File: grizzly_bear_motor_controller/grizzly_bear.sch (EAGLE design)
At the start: 54 parts, among them Q1 PH7030L, Q2 PH7030L, Q3 PH7030L, Q4 PH7030L, Q5 FDD4141TO252, U1 A4940, U2 ATMEGA32U4-AU, U3 ACS714, U4 UA78L00, Y1 16MHz

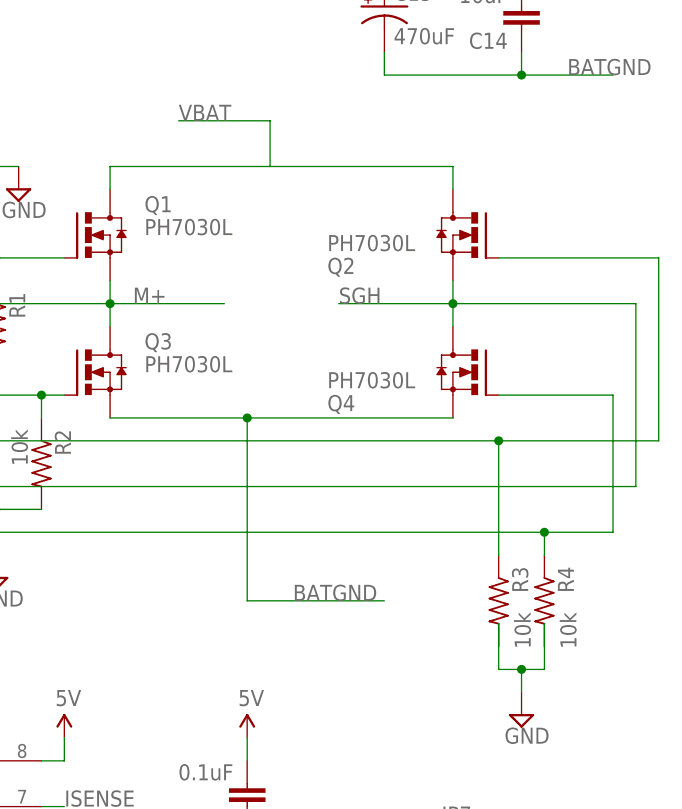
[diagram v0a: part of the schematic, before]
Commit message: Fix mistake with AHI shorted to ENC2
Change-Id: I23787c04aa77e54cc0262fec6cb01ab894f515dc
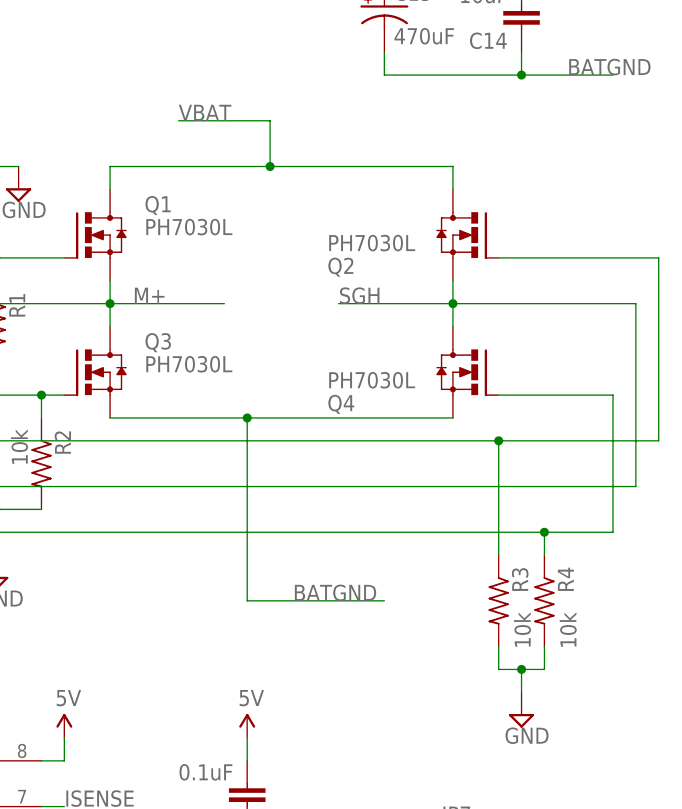
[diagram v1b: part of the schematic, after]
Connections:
- new net AHI: R13.1, U1.AHI, U2.(PCINT6/OC1B/OC4B/ADC13)PB6
- net ENC2: no longer R13.1, U1.AHI, U2.(PCINT6/OC1B/OC4B/ADC13)PB6
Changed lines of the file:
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@@
 <pinref part="Q2" gate="G$1" pin="D"/>
 <wire x1="132.08" y1="93.98" x2="132.08" y2="96.52" width="0.1524" layer="91"/>
+<junction x="111.76" y="96.52"/>
 </segment>
 <segment>
@@
 <wire x1="139.7" y1="40.64" x2="137.16" y2="40.64" width="0.1524" layer="91"/>
 <pinref part="R3" gate="G$1" pin="2"/>
-<wire x1="137.16" y1="45.72" x2="137.16" y2="43.18" width="0.1524" layer="91"/>
 <wire x1="137.16" y1="40.64" x2="137.16" y2="43.18" width="0.1524" layer="91"/>
 <pinref part="R4" gate="G$1" pin="2"/>
-<wire x1="142.24" y1="45.72" x2="142.24" y2="43.18" width="0.1524" layer="91"/>
 <wire x1="142.24" y1="43.18" x2="142.24" y2="40.64" width="0.1524" layer="91"/>
 <wire x1="142.24" y1="40.64" x2="139.7" y2="40.64" width="0.1524" layer="91"/>
@@
 </segment>
 <segment>
-<wire x1="5.08" y1="71.12" x2="15.24" y2="71.12" width="0.1524" layer="91"/>
-<wire x1="15.24" y1="71.12" x2="15.24" y2="81.28" width="0.1524" layer="91"/>
-<wire x1="15.24" y1="81.28" x2="25.4" y2="81.28" width="0.1524" layer="91"/>
-<pinref part="U1" gate="G$1" pin="AHI"/>
-<pinref part="R13" gate="G$1" pin="1"/>
-<wire x1="5.08" y1="58.42" x2="5.08" y2="71.12" width="0.1524" layer="91"/>
-<wire x1="5.08" y1="71.12" x2="-2.54" y2="71.12" width="0.1524" layer="91"/>
-<wire x1="-2.54" y1="71.12" x2="-5.08" y2="68.58" width="0.1524" layer="91"/>
-<wire x1="-5.08" y1="68.58" x2="-10.16" y2="68.58" width="0.1524" layer="91"/>
-<junction x="5.08" y="71.12"/>
-<pinref part="U2" gate="G$1" pin="(PCINT6/OC1B/OC4B/ADC13)PB6"/>
-</segment>
-<segment>
 <wire x1="-10.16" y1="73.66" x2="-7.62" y2="73.66" width="0.1524" layer="91"/>
 <label x="-7.62" y="73.66" size="1.778" layer="95"/>
@@
 </segment>
 </net>
+<net name="AHI" class="0">
+<segment>
+<wire x1="5.08" y1="71.12" x2="15.24" y2="71.12" width="0.1524" layer="91"/>
+<wire x1="15.24" y1="71.12" x2="15.24" y2="81.28" width="0.1524" layer="91"/>
+<wire x1="15.24" y1="81.28" x2="25.4" y2="81.28" width="0.1524" layer="91"/>
+<pinref part="U1" gate="G$1" pin="AHI"/>
+<pinref part="R13" gate="G$1" pin="1"/>
+<wire x1="5.08" y1="58.42" x2="5.08" y2="71.12" width="0.1524" layer="91"/>
+<wire x1="5.08" y1="71.12" x2="-2.54" y2="71.12" width="0.1524" layer="91"/>
+<wire x1="-2.54" y1="71.12" x2="-5.08" y2="68.58" width="0.1524" layer="91"/>
+<wire x1="-5.08" y1="68.58" x2="-10.16" y2="68.58" width="0.1524" layer="91"/>
+<junction x="5.08" y="71.12"/>
+<pinref part="U2" gate="G$1" pin="(PCINT6/OC1B/OC4B/ADC13)PB6"/>
+</segment>
+</net>

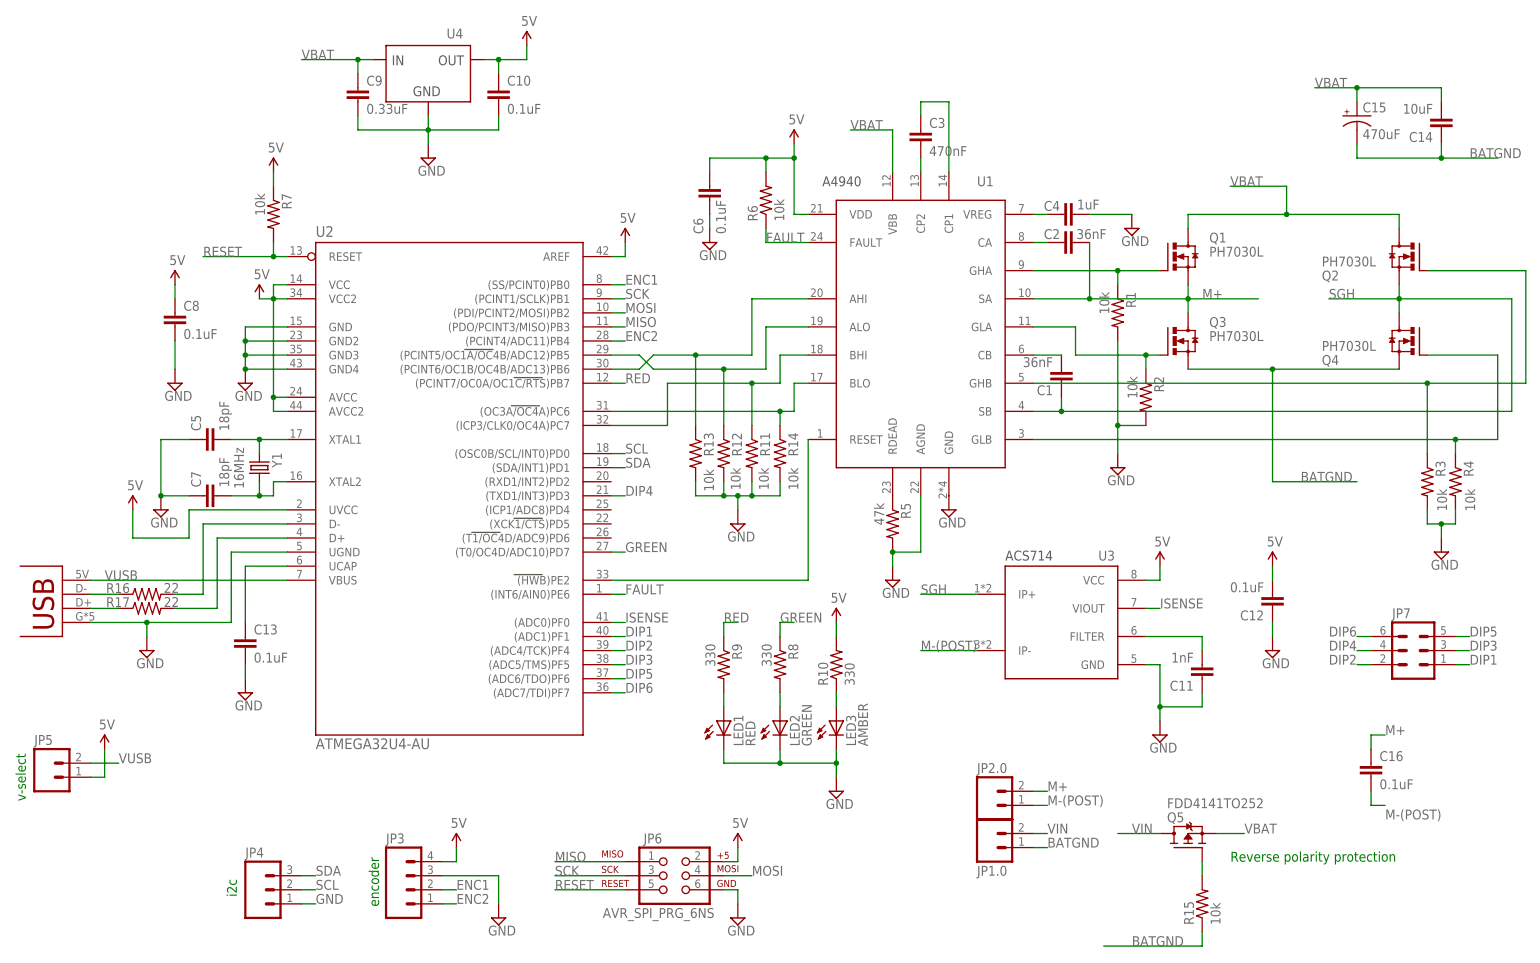
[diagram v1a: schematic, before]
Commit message: Fix 18pF caps and renumber all passives
Change-Id: Id4e7dc3682557a51dcb971b0b6fbe1525da739df
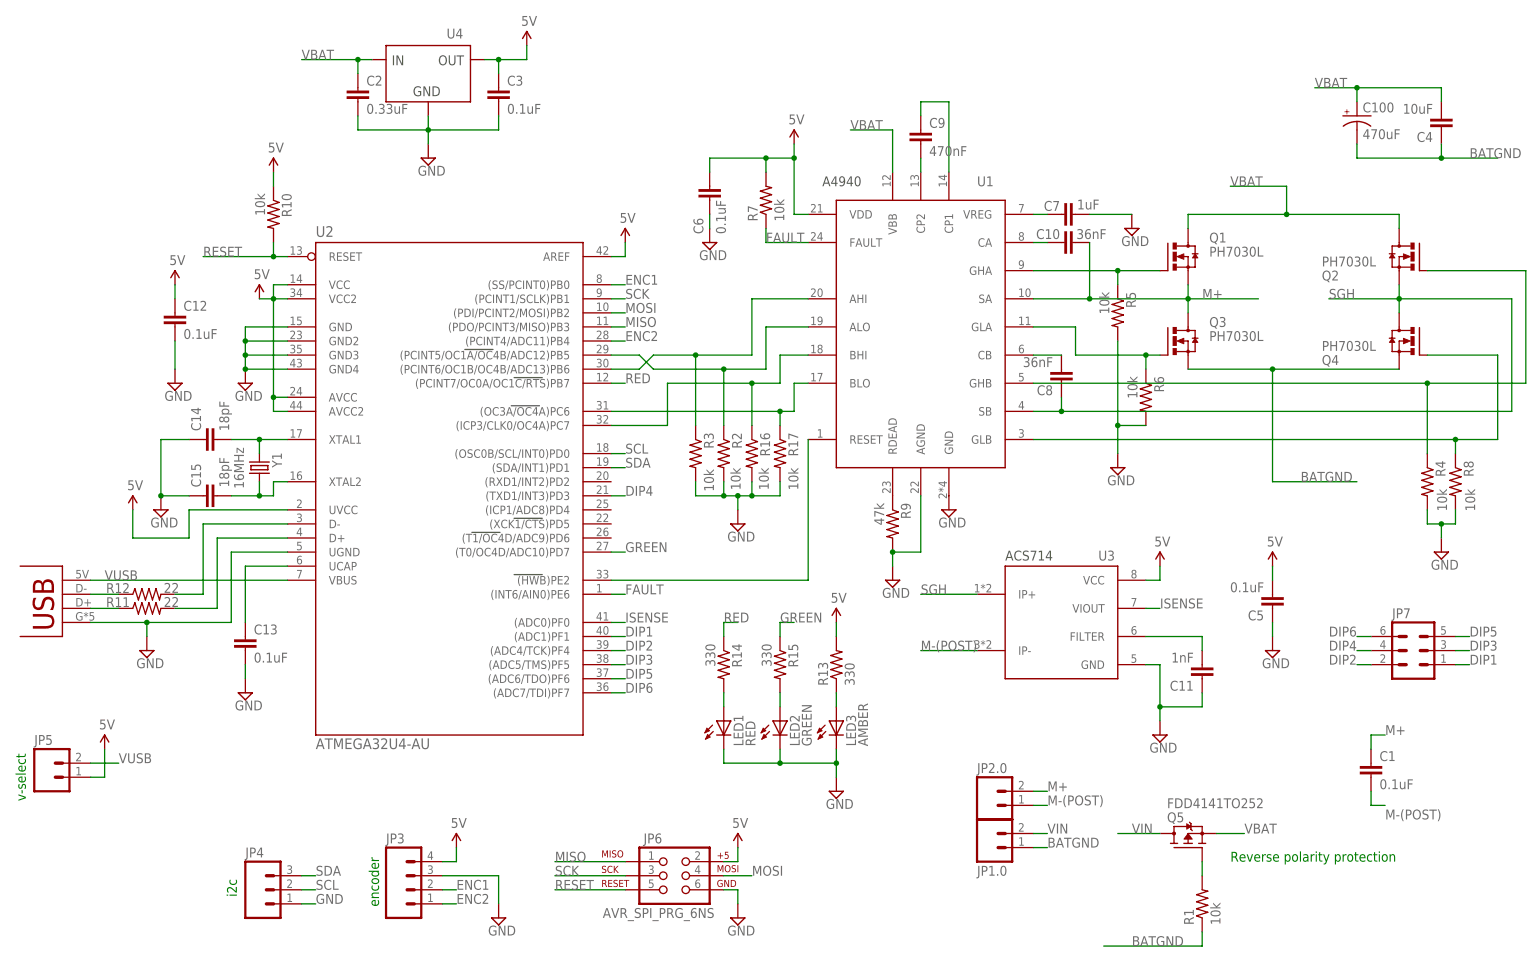
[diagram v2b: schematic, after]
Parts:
- removed C16: 0.1uF, SparkFun-Passives:CAP0603-CAP
- added C100: 470uF, SparkFun-Passives:CAP_POLG
- C1: value 36nF -> 0.1uF
- C10, C8: value 0.1uF -> 36nF
- C14: value 10uF -> 18pF
- C15: value 470uF -> 18pF; device SparkFun-Passives:CAP_POLG -> SparkFun-Passives:CAP0603-CAP
- C2: value 36nF -> 0.33uF
- C3: value 470nF -> 0.1uF
- C4: value 1uF -> 10uF
- C5: value 18pF -> 0.1uF
- C7: value 18pF -> 1uF
- C9: value 0.33uF -> 470nF
- R10: value 330 -> 10k; device resistor:R-US_R0603 -> rcl:R-US_R0603
- R11, R12: value 10k -> 22; device resistor:R-US_R0603 -> rcl:R-US_R0603
- R13, R14, R15: value 10k -> 330
- R16, R17: value 22 -> 10k; device rcl:R-US_R0603 -> resistor:R-US_R0603
- R5: value 47k -> 10k
- R7: device rcl:R-US_R0603 -> resistor:R-US_R0603
- R8: value 330 -> 10k
- R9: value 330 -> 47k
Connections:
- net 5V: now also C12.1, C3.1, C5.2, R10.1, R13.2, R7.2; no longer C10.1, C12.2, C8.1, R10.2, R6.2, R7.1
- net AHI: now also R3.1; no longer R13.1
- net BATGND: now also C100.-, C4.1, R1.1; no longer C14.1, C15.-, R15.1
- net FAULT: now also R7.1; no longer R6.1
- net GND: now also C12.2, C14.1, C15.1, C2.2, C3.2, C7.2, R16.2, R17.2, R6.2, R8.2, R9.2; no longer C10.2, C12.1, C4.2, C7.1, C8.2, C9.2, R1.2, R11.2, R12.2, R13.2, R14.2
- net GREEN: now also R15.1; no longer R8.1
- net M+: now also C1.1, C10.2; no longer C16.1, C2.2
- net M-(POST): now also C1.2; no longer C16.2
- net N$1: now also R1.2; no longer R15.2
- net N$11: now also R8.1; no longer R4.1
- net N$13: now also R4.1; no longer R3.1
- net N$14: now also C8.2; no longer C1.2
- net N$16: now also C10.1; no longer C2.1
- net N$17: now also C7.1; no longer C4.1
- net N$19: now also C9.1; no longer C3.1
- net N$2: now also R5.1; no longer R1.1
- net N$20: now also R17.1; no longer R14.1
- net N$21: now also R16.1; no longer R11.1
- net N$22: now also R2.1; no longer R12.1
- net N$23: now also R14.2; no longer R9.2
- net N$24: now also R11.1; no longer R17.1
- net N$25: now also R13.1; no longer R10.1
- net N$26: now also C14.2; no longer C5.2
- net N$27: now also C15.2; no longer C7.2
- net N$29: now also R12.1; no longer R16.1
- net N$3: now also C9.2; no longer C3.2
- net N$5: now also R15.2; no longer R8.2
- net N$6: now also R9.1; no longer R5.1
- net N$7: now also R12.2; no longer R16.2
- net N$8: now also R6.1; no longer R2.1
- net N$9: now also R11.2; no longer R17.2
- net RED: now also R14.1; no longer R9.1
- net RESET: now also R10.2; no longer R7.2
- net SGH: now also C8.1; no longer C1.1
- net VBAT: now also C100.+, C2.1, C4.2; no longer C14.2, C15.+, C9.1
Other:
- moved on the sheet: C1, C10, C12, C14, C2, C3, C4, C5, C7, C8, C9, R1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

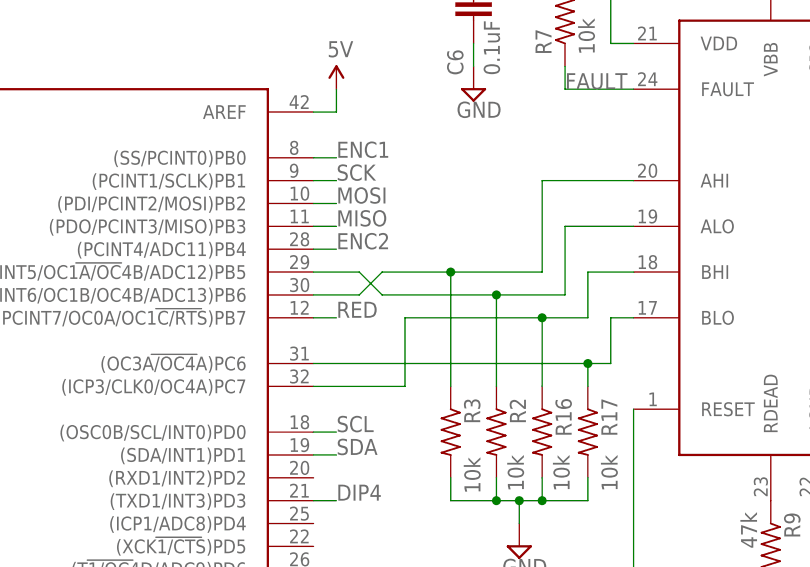
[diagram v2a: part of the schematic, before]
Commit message: Swap PWM pins on one side of bridge to allow locked-antiphase PWM.
Change-Id: I960fdec47b52c005c589c20b71f3d1438955e5d5
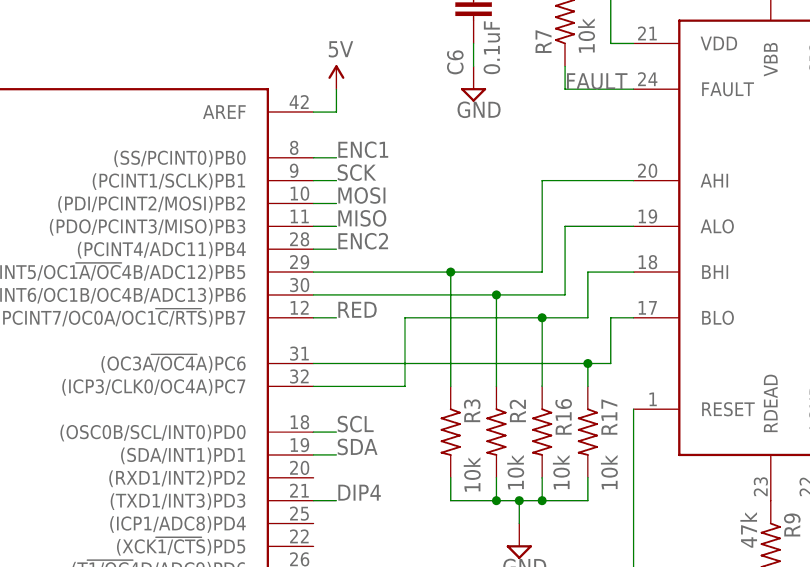
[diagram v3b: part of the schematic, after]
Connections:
- net AHI: now also U2.(PCINT5/OC1A/OC4B/ADC12)PB5; no longer U2.(PCINT6/OC1B/OC4B/ADC13)PB6
- net N$22: now also U2.(PCINT6/OC1B/OC4B/ADC13)PB6; no longer U2.(PCINT5/OC1A/OC4B/ADC12)PB5
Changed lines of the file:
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@@
 <pinref part="R2" gate="G$1" pin="1"/>
 <wire x1="10.16" y1="58.42" x2="10.16" y2="68.58" width="0.1524" layer="91"/>
-<wire x1="10.16" y1="68.58" x2="-2.54" y2="68.58" width="0.1524" layer="91"/>
-<wire x1="-2.54" y1="68.58" x2="-5.08" y2="71.12" width="0.1524" layer="91"/>
-<wire x1="-5.08" y1="71.12" x2="-10.16" y2="71.12" width="0.1524" layer="91"/>
+<wire x1="10.16" y1="68.58" x2="-10.16" y2="68.58" width="0.1524" layer="91"/>
 <junction x="10.16" y="68.58"/>
-<pinref part="U2" gate="G$1" pin="(PCINT5/OC1A/OC4B/ADC12)PB5"/>
+<pinref part="U2" gate="G$1" pin="(PCINT6/OC1B/OC4B/ADC13)PB6"/>
 </segment>
 </net>
@@
 <pinref part="R3" gate="G$1" pin="1"/>
 <wire x1="5.08" y1="58.42" x2="5.08" y2="71.12" width="0.1524" layer="91"/>
-<wire x1="5.08" y1="71.12" x2="-2.54" y2="71.12" width="0.1524" layer="91"/>
-<wire x1="-2.54" y1="71.12" x2="-5.08" y2="68.58" width="0.1524" layer="91"/>
-<wire x1="-5.08" y1="68.58" x2="-10.16" y2="68.58" width="0.1524" layer="91"/>
 <junction x="5.08" y="71.12"/>
-<pinref part="U2" gate="G$1" pin="(PCINT6/OC1B/OC4B/ADC13)PB6"/>
-</segment>
-</net>
+<pinref part="U2" gate="G$1" pin="(PCINT5/OC1A/OC4B/ADC12)PB5"/>
+<wire x1="5.08" y1="71.12" x2="-10.16" y2="71.12" width="0.1524" layer="91"/>
+</segment>
+</net>

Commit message: Expand pad of big capacitor
Change-Id: I42f40d14e226f23feeab3faabe0e8d13880d1d3c
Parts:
- C100: device SparkFun-Passives:CAP_POLG -> pie:CAP_POLG
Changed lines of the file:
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@@
 <layers>
 <layer number="1" name="Top" color="4" fill="1" visible="yes" active="no"/>
-<layer number="2" name="Route2" color="1" fill="3" visible="no" active="no"/>
-<layer number="3" name="Route3" color="4" fill="3" visible="no" active="no"/>
-<layer number="4" name="Route4" color="1" fill="4" visible="no" active="no"/>
-<layer number="5" name="Route5" color="4" fill="4" visible="no" active="no"/>
-<layer number="6" name="Route6" color="1" fill="8" visible="no" active="no"/>
-<layer number="7" name="Route7" color="4" fill="8" visible="no" active="no"/>
-<layer number="8" name="Route8" color="1" fill="2" visible="no" active="no"/>
-<layer number="9" name="Route9" color="4" fill="2" visible="no" active="no"/>
-<layer number="10" name="Route10" color="1" fill="7" visible="no" active="no"/>
-<layer number="11" name="Route11" color="4" fill="7" visible="no" active="no"/>
-<layer number="12" name="Route12" color="1" fill="5" visible="no" active="no"/>
-<layer number="13" name="Route13" color="4" fill="5" visible="no" active="no"/>
-<layer number="14" name="Route14" color="1" fill="6" visible="no" active="no"/>
-<layer number="15" name="Route15" color="4" fill="6" visible="no" active="no"/>
+<layer number="2" name="Route2" color="1" fill="3" visible="yes" active="no"/>
+<layer number="3" name="Route3" color="4" fill="3" visible="yes" active="no"/>
+<layer number="4" name="Route4" color="1" fill="4" visible="yes" active="no"/>
+<layer number="5" name="Route5" color="4" fill="4" visible="yes" active="no"/>
+<layer number="6" name="Route6" color="1" fill="8" visible="yes" active="no"/>
+<layer number="7" name="Route7" color="4" fill="8" visible="yes" active="no"/>
+<layer number="8" name="Route8" color="1" fill="2" visible="yes" active="no"/>
+<layer number="9" name="Route9" color="4" fill="2" visible="yes" active="no"/>
+<layer number="10" name="Route10" color="1" fill="7" visible="yes" active="no"/>
+<layer number="11" name="Route11" color="4" fill="7" visible="yes" active="no"/>
+<layer number="12" name="Route12" color="1" fill="5" visible="yes" active="no"/>
+<layer number="13" name="Route13" color="4" fill="5" visible="yes" active="no"/>
+<layer number="14" name="Route14" color="1" fill="6" visible="yes" active="no"/>
+<layer number="15" name="Route15" color="4" fill="6" visible="yes" active="no"/>
 <layer number="16" name="Bottom" color="1" fill="1" visible="yes" active="no"/>
 <layer number="17" name="Pads" color="2" fill="1" visible="yes" active="no"/>
@@
 <part name="SUPPLY17" library="supply2" deviceset="GND" device=""/>
 <part name="C4" library="SparkFun-Passives" deviceset="CAP" device="0603-CAP" value="10uF"/>
-<part name="C100" library="SparkFun-Passives" deviceset="CAP_POL" device="G" value="470uF"/>
 <part name="Q5" library="transistor-fet" deviceset="FDD4141" device="TO252"/>
 <part name="R1" library="resistor" deviceset="R-US_" device="R0603" value="10k"/>
@@
 <part name="JP7" library="con-lstb" deviceset="MA03-2" device=""/>
 <part name="U$14" library="SparkFun-Aesthetics" deviceset="5V" device=""/>
+<part name="C100" library="pie" deviceset="CAP_POL" device="G" value="470uF"/>
 </parts>
 <sheets>
@@
 <instance part="SUPPLY17" gate="GND" x="12.7" y="40.64"/>
 <instance part="C4" gate="G$1" x="139.7" y="114.3" rot="R180"/>
-<instance part="C100" gate="G$1" x="124.46" y="114.3"/>
 <instance part="Q5" gate="G$1" x="93.98" y="-17.78" smashed="yes" rot="MR90">
 <attribute name="VALUE" x="90.17" y="-8.89" size="1.778" layer="96" rot="MR180"/>
@@
 <instance part="JP7" gate="1" x="134.62" y="17.78"/>
 <instance part="U$14" gate="G$1" x="-25.4" y="127"/>
+<instance part="C100" gate="G$1" x="124.46" y="114.3"/>
 </instances>
 <busses>
@@
 </segment>
 <segment>
-<wire x1="124.46" y1="116.84" x2="124.46" y2="119.38" width="0.1524" layer="91"/>
 <label x="116.84" y="119.38" size="1.778" layer="95"/>
 <pinref part="C4" gate="G$1" pin="2"/>
@@
 <junction x="124.46" y="119.38"/>
 <pinref part="C100" gate="G$1" pin="+"/>
+<wire x1="124.46" y1="116.84" x2="124.46" y2="119.38" width="0.1524" layer="91"/>
 </segment>
 <segment>
@@
 <segment>
 <pinref part="C4" gate="G$1" pin="1"/>
-<wire x1="124.46" y1="106.68" x2="124.46" y2="109.22" width="0.1524" layer="91"/>
 <wire x1="139.7" y1="109.22" x2="139.7" y2="106.68" width="0.1524" layer="91"/>
 <wire x1="139.7" y1="106.68" x2="124.46" y2="106.68" width="0.1524" layer="91"/>
-<pinref part="C100" gate="G$1" pin="-"/>
 <wire x1="139.7" y1="106.68" x2="149.86" y2="106.68" width="0.1524" layer="91"/>
 <junction x="139.7" y="106.68"/>
 <label x="144.78" y="106.68" size="1.778" layer="95"/>
-</segment>
-<segment>
+<pinref part="C100" gate="G$1" pin="-"/>
+<wire x1="124.46" y1="109.22" x2="124.46" y2="106.68" width="0.1524" layer="91"/>
+</segment>
+<segment>
